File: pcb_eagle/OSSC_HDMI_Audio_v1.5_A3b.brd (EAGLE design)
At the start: 29.8 x 17 mm, 29 parts, among them U1 PCM1808, U2 74LVC1G34, U3 MK2507SLF

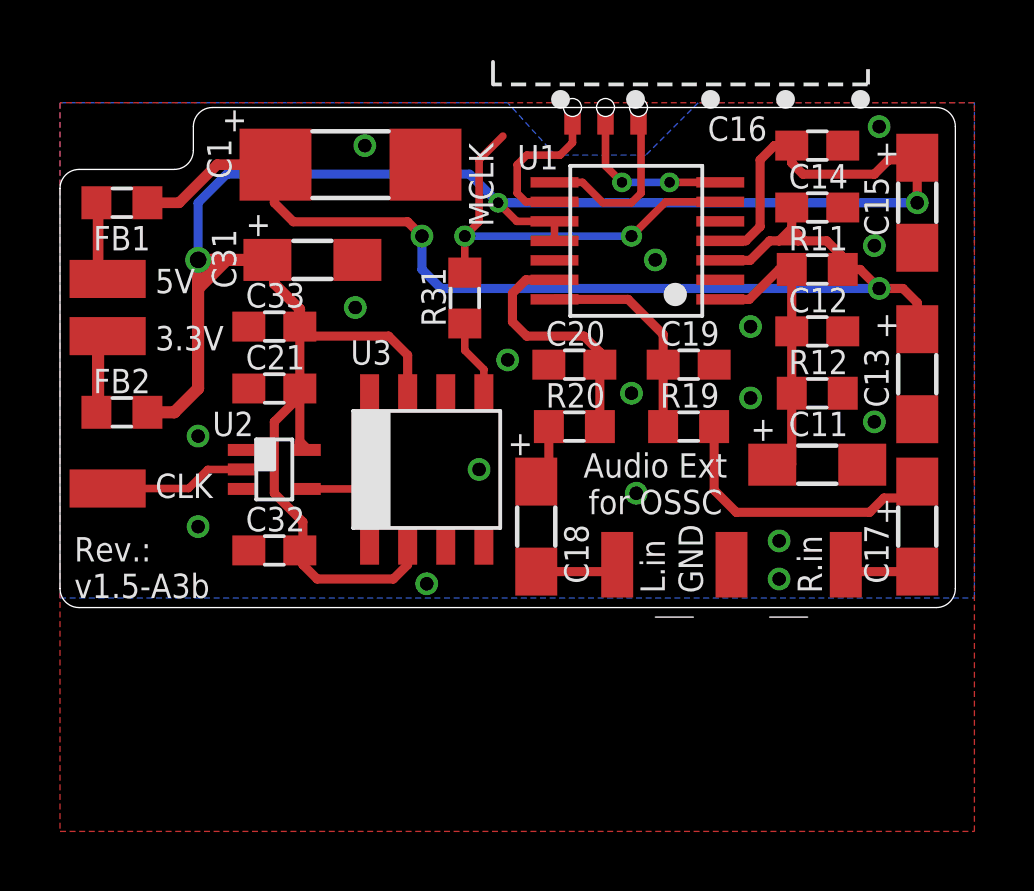
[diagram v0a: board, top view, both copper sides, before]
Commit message: Fix: remove needless wire and silkscreen from PCB
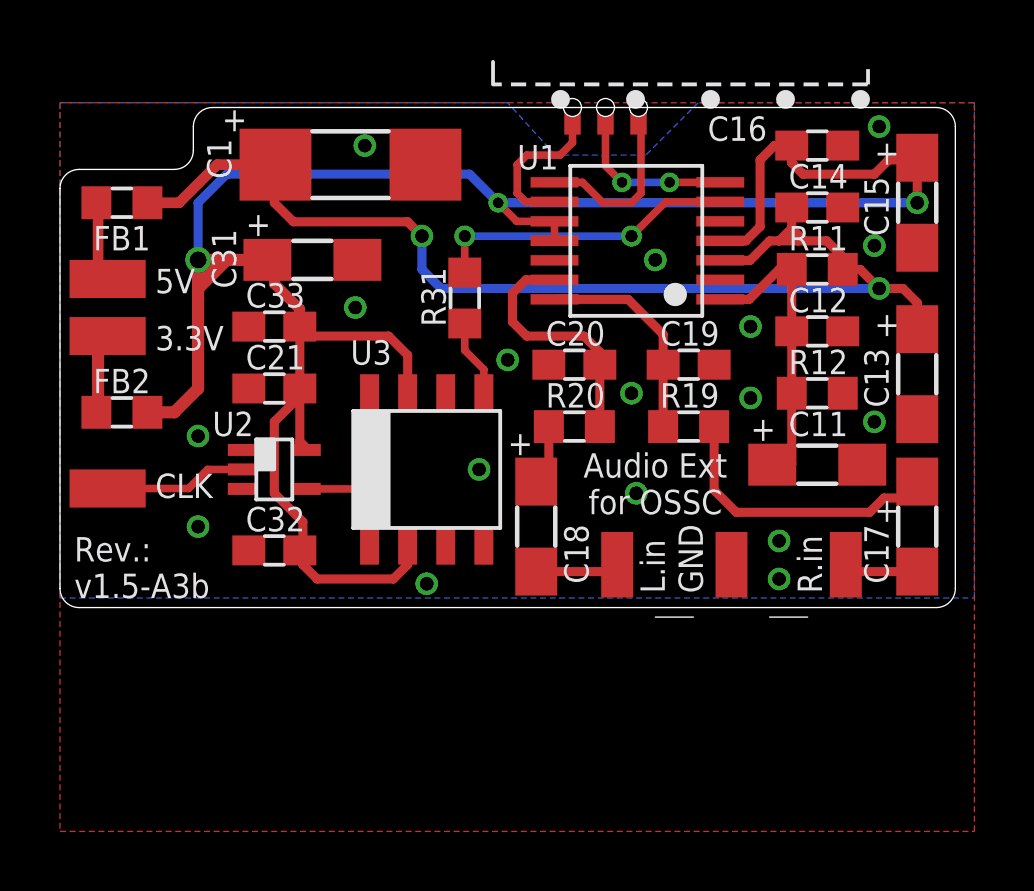
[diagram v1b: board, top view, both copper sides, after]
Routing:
- net N$17: track 14.1 -> 10.2 mm
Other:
- board text removed: "MCLK"
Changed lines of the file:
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@@
 <vertex x="29.5275" y="23.97125"/>
 </polygon>
-<text x="14.44625" y="20.16125" size="0.8128" layer="25" font="vector" ratio="15" rot="R90">MCLK</text>
 <wire x1="29.845" y1="8.09625" x2="29.21" y2="7.46125" width="0" layer="20" curve="-90"/>
 </plain>
@@
 <wire x1="22.00875" y1="20.985" x2="20.19125" y2="20.985" width="0.254" layer="1"/>
 <wire x1="20.19125" y1="20.985" x2="19.05" y2="19.84375" width="0.254" layer="1"/>
-<wire x1="13.49375" y1="19.84375" x2="13.97" y2="20.32" width="0.254" layer="1"/>
-<wire x1="13.97" y1="20.32" x2="13.97" y2="22.38375" width="0.254" layer="1"/>
-<wire x1="13.97" y1="22.38375" x2="14.76375" y2="23.1775" width="0.254" layer="1"/>
 </signal>
 <signal name="VCC/2">
